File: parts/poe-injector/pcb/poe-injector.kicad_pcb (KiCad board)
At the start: 2 copper layers, 58.4 x 30.9 mm, 17 parts, among them J1 Conn_01x01_Shielded, SW2 SW_SPDT

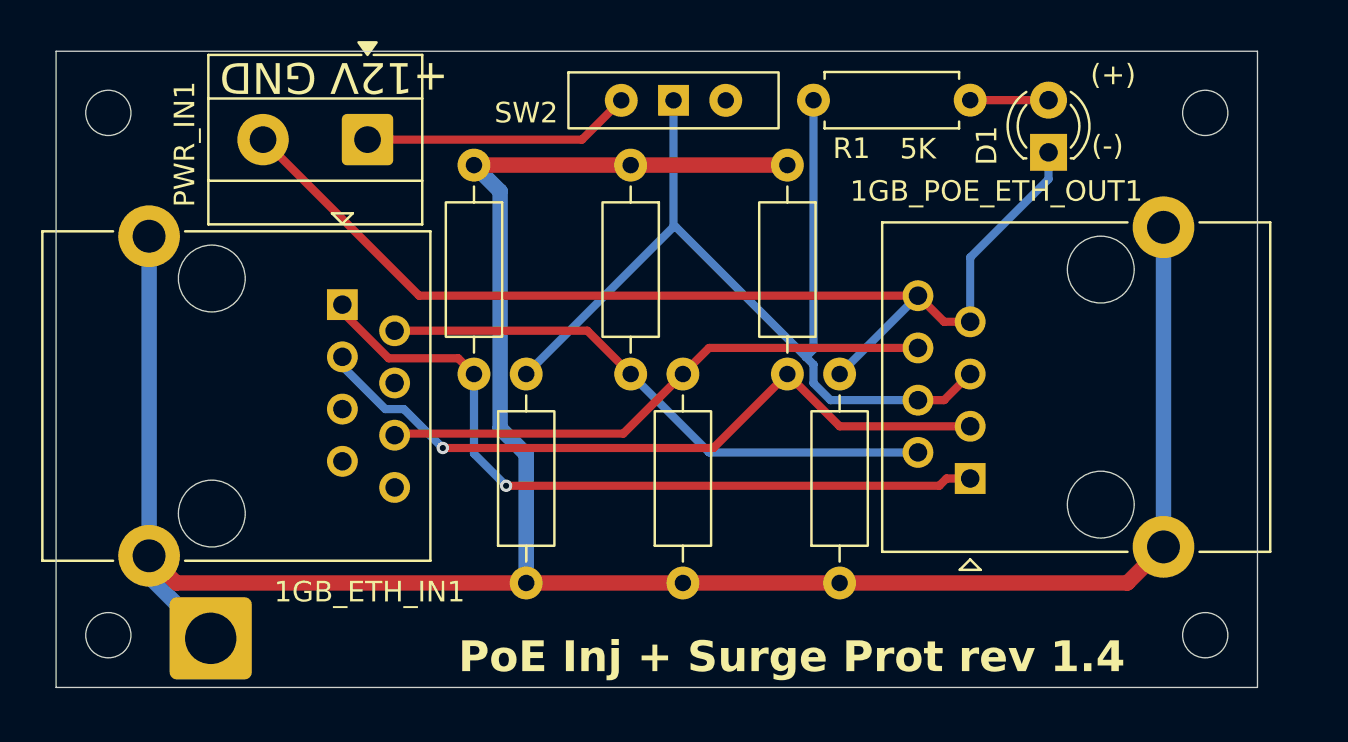
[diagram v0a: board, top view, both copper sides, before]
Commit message: update RJ45 connector footprint to the 'clip up' component that I finally found.
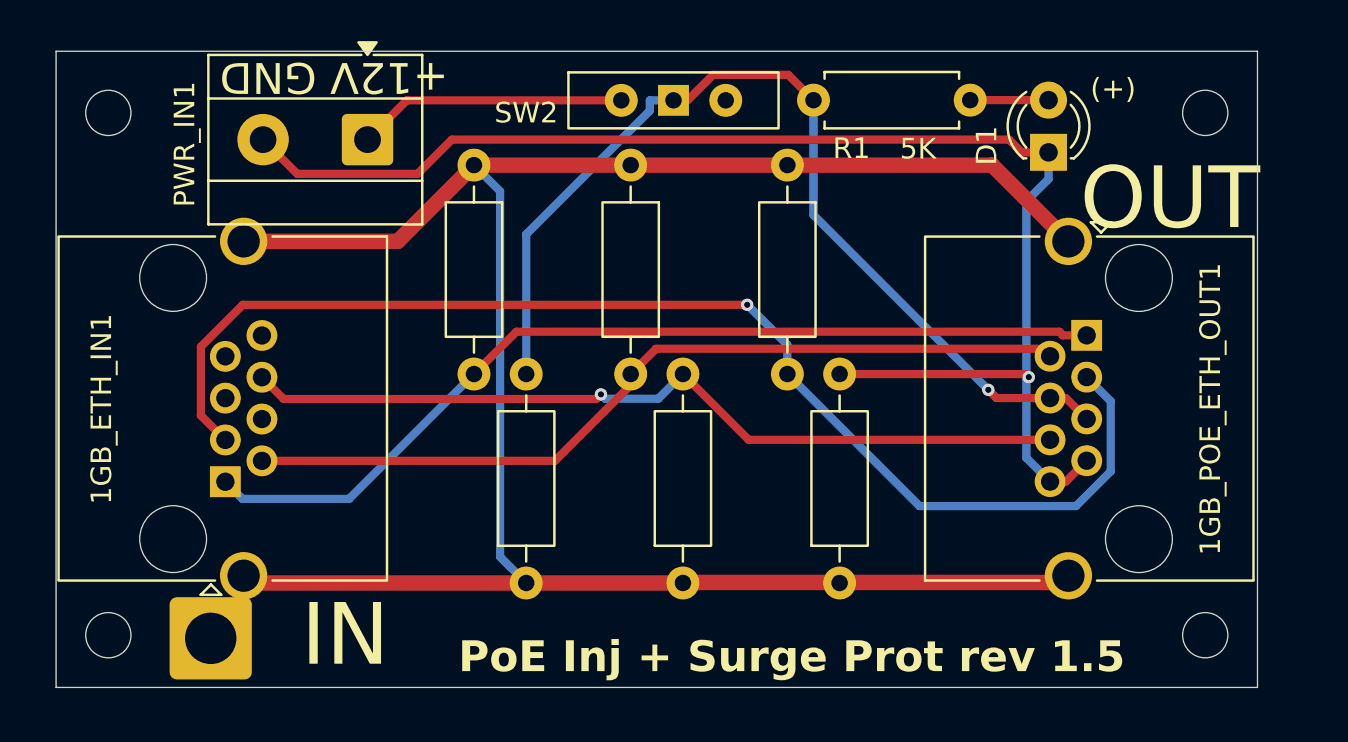
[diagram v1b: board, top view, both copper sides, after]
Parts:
- 1GB_ETH_IN1, 1GB_POE_ETH_OUT1: footprint Connector_RJ:RJ45_Ninigi_GE -> Connector_RJ:RJ45_Amphenol_RJHSE5380
- moved 1GB_ETH_IN1 10.3 mm to (76.8, 40.8), turned to 90 degrees
- moved 1GB_POE_ETH_OUT1 8.98 mm to (118.7, 33.7), turned to -90 degrees
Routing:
- net Net-(1GB_ETH_IN1-Pad3): track 35.2 -> 60.8 mm
- net Earth: track 123.5 -> 105.9 mm
- net GND: track 53.3 -> 68.3 mm, vias 0 -> 1
- net Net-(1GB_ETH_IN1-Pad6): track 27.2 -> 40.8 mm, vias 0 -> 1
- net Net-(1GB_ETH_IN1-Pad2): track 27.9 -> 40.0 mm
- net Net-(1GB_ETH_IN1-Pad1): track 36.8 -> 45.7 mm, vias 1 -> 0
- net Net-(SW2-A): track 47.9 -> 47.8 mm, vias 0 -> 1
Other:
- board text added: "IN"
- board text added: "OUT"
- board text added: "PoE Inj + Surge Prot rev 1.5"
- board text removed: "(-)"
- board text removed: "PoE Inj + Surge Prot rev 1.4"
